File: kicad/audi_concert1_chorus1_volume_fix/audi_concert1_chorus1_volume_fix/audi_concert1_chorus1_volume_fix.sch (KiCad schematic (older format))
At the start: 39 parts, among them CON1 I2C_to_TDA, CON2 USB, CON3 SPI_TO_PANEL, CON4 JLINK, SW1 SWITCH_DPST, U1 68HC05_PLCC, U2 AP1117-33, U3 STM32F030C8Tx, Y1 Crystal_GND24, Y2 Crystal_GND24

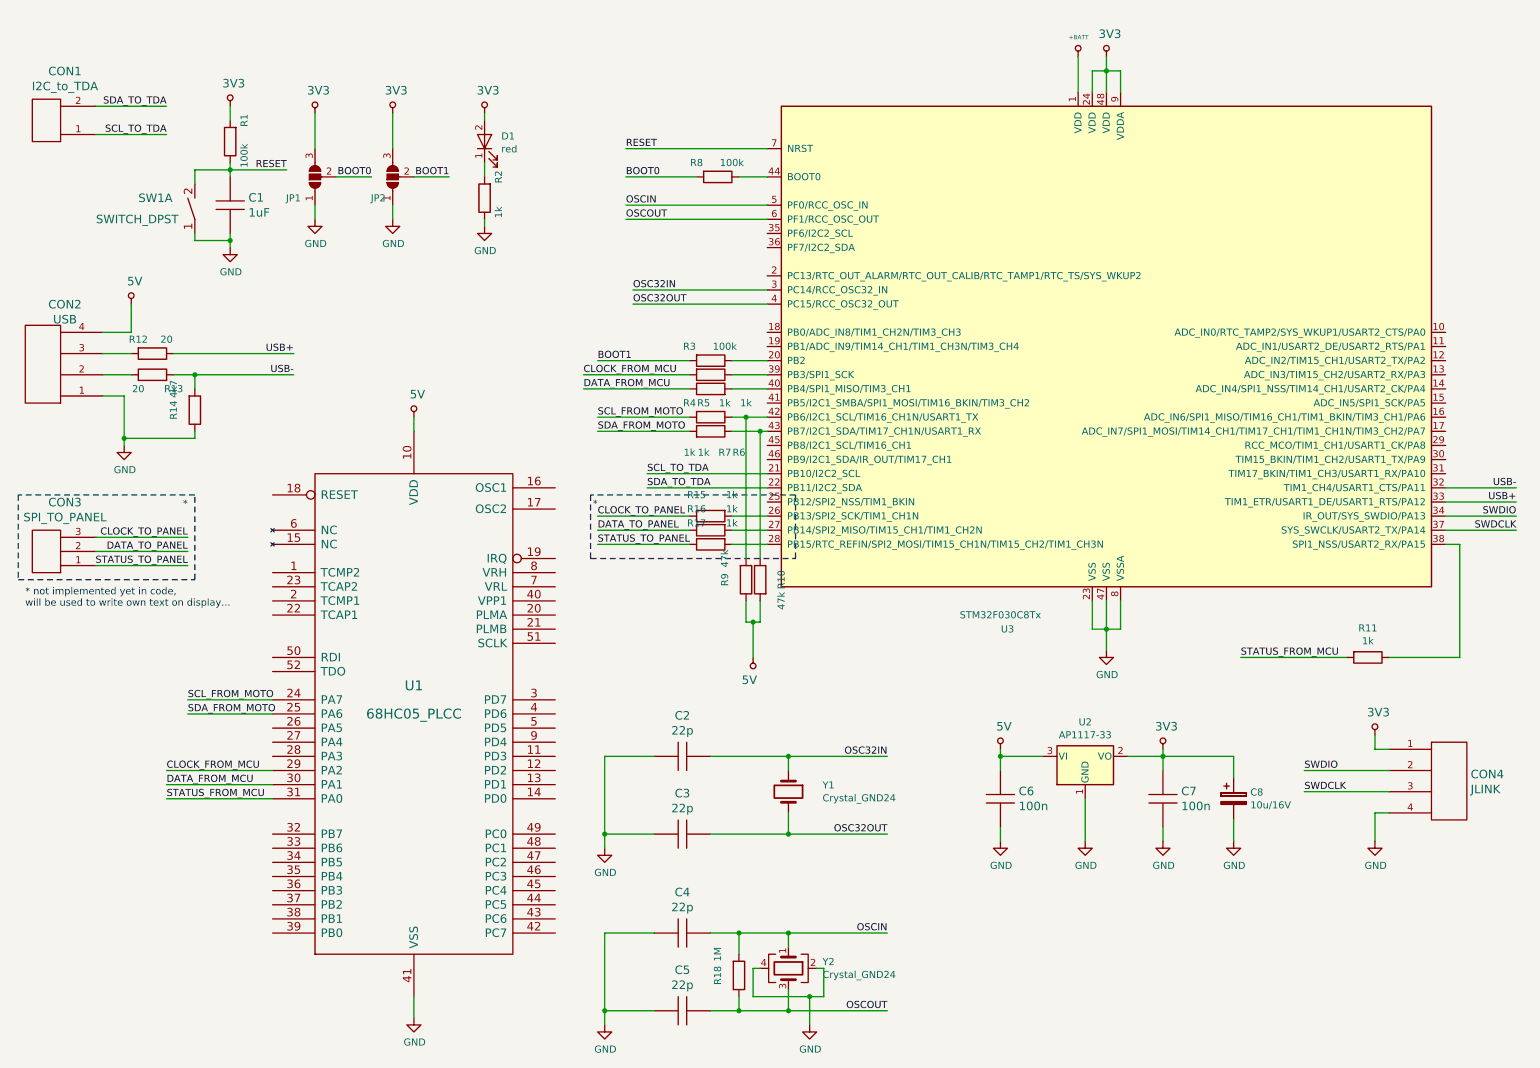
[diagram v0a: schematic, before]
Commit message: moved to separed repository audi_concert1_chorus1_volume_fix
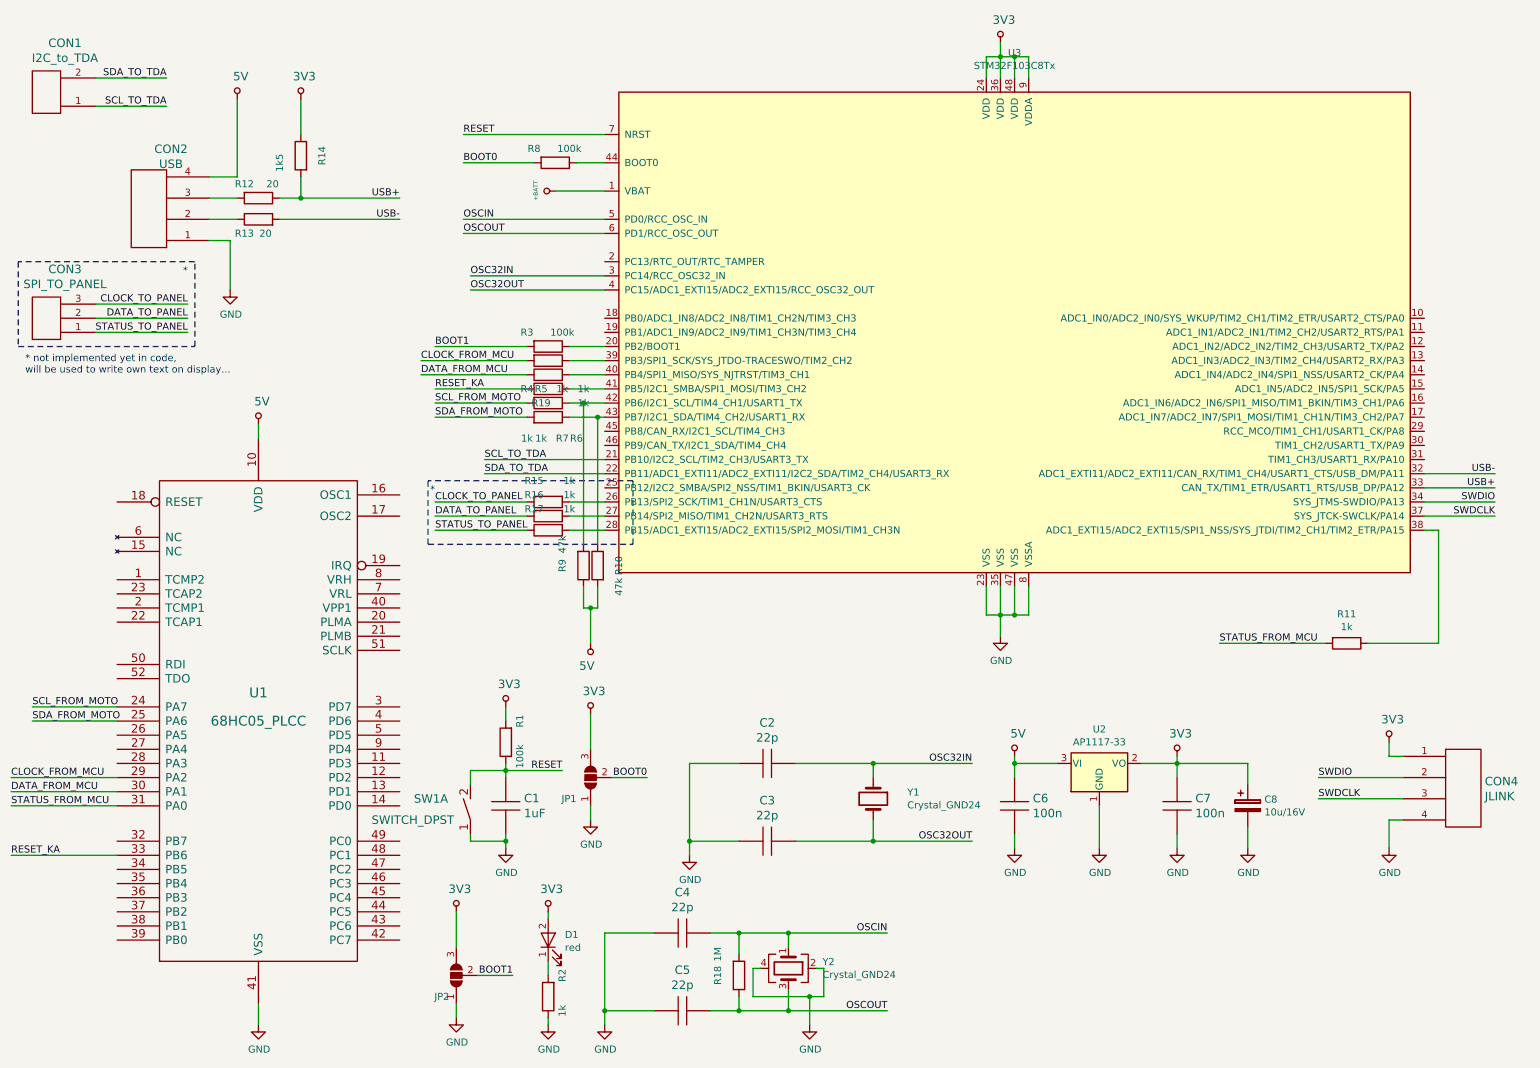
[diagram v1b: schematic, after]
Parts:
- removed U3: STM32F030C8Tx, Housings_QFP:LQFP-48_7x7mm_Pitch0.5mm, symbol MCU_ST_STM32:STM32F030C8Tx
- added R19: 1k, Resistors_SMD.pretty:R_0805_HandSoldering, symbol Device:R
- added U3: STM32F103C8Tx, Housings_QFP:LQFP-48_7x7mm_Pitch0.5mm, symbol MCU_ST_STM32:STM32F103C8Tx
- C8: footprint Capacitors_Tantalum_SMD.pretty:CP_Tantalum_Case-A_EIA-3216-18_Hand -> Capacitors_Tantalum_SMD.pretty:TantalC_SizeA_EIA-3216_HandSoldering
- R14: value 4k7 -> 1k5
- SW1: footprint (none) -> modules:3x6x2.5mm_tact_switch
- U1: footprint SMD_Packages.pretty:PLCC-52 -> modules:PLCC-52_mirrored
- U2: footprint modules:SOT-223-REGULATOR -> ab2_sot.mod:AB2_SOT223
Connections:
- net +BATT: now also U3.1 (VBAT)
- net 3V3: now also R14.1, U3.24 (VDD), U3.36 (VDD), U3.48 (VDD), U3.9 (VDDA)
- net GND: now also U3.23 (VSS), U3.35 (VSS), U3.47 (VSS), U3.8 (VSSA); no longer R14.1
- net OSC32IN: now also U3.3 (PC14/RCC_OSC32_IN)
- net OSC32OUT: now also U3.4 (PC15/ADC1_EXTI15/ADC2_EXTI15/RCC_OSC32_OUT)
- net OSCIN: now also U3.5 (PD0/RCC_OSC_IN)
- net OSCOUT: now also U3.6 (PD1/RCC_OSC_OUT)
- net RESET: now also U3.7 (NRST)
- net SCL_TO_TDA: now also U3.21 (PB10/I2C2_SCL/TIM2_CH3/USART3_TX)
- net SDA_TO_TDA: now also U3.22 (PB11/ADC1_EXTI11/ADC2_EXTI11/I2C2_SDA/TIM2_CH4/USART3_RX)
- net SWDCLK: now also U3.37 (SYS_JTCK-SWCLK/PA14)
- net SWDIO: now also U3.34 (SYS_JTMS-SWDIO/PA13)
- net USB+: now also R14.2, U3.33 (CAN_TX/TIM1_ETR/USART1_RTS/USB_DP/PA12)
- net USB-: now also U3.32 (ADC1_EXTI11/ADC2_EXTI11/CAN_RX/TIM1_CH4/USART1_CTS/USB_DM/PA11); no longer R14.2
- net at R3.1: now also U3.20 (PB2/BOOT1)
- net at R15.2: now also U3.26 (PB13/SPI2_SCK/TIM1_CH1N/USART3_CTS)
- net at R16.2: now also U3.27 (PB14/SPI2_MISO/TIM1_CH2N/USART3_RTS)
- net at R17.2: now also U3.28 (PB15/ADC1_EXTI15/ADC2_EXTI15/SPI2_MOSI/TIM1_CH3N)
- net at R11.1: now also U3.38 (ADC1_EXTI15/ADC2_EXTI15/SPI1_NSS/SYS_JTDI/TIM2_CH1/TIM2_ETR/PA15)
- net at R4.1: now also U3.39 (PB3/SPI1_SCK/SYS_JTDO-TRACESWO/TIM2_CH2)
- net at R5.2: now also U3.40 (PB4/SPI1_MISO/SYS_NJTRST/TIM3_CH1)
- net at R6.1, R9.2: now also U3.42 (PB6/I2C1_SCL/TIM4_CH1/USART1_TX)
- net at R10.1, R7.1: now also U3.43 (PB7/I2C1_SDA/TIM4_CH2/USART1_RX)
- net at R8.1: now also U3.44 (BOOT0)
- net RESET_KA: now reaches U1.33 (PB6)
- net RESET_KA: now also R19.1
- new net: R19.2, U3.41 (PB5/I2C1_SMBA/SPI1_MOSI/TIM3_CH2)
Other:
- moved on the sheet: C1, C2, C3, C6, C7, C8, CON1, CON2, CON3, CON4, D1, JP1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
